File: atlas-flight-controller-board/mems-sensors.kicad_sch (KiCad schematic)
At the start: 11 parts, among them IC1 LSM6DSV80XTR, IC2 LPS22HHTR, U1 LIS2MDL

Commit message: Bare Schematic (No LEDS, etc added) finished. Begin PCB Layout.
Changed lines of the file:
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@@
+	)
+	(no_connect
+		(at 95.25 158.75)
+	)
+	(no_connect
+		(at 95.25 163.83)
+	)
+	(no_connect
+		(at 95.25 161.29)
 	)
 	(no_connect
 		(at 99.06 62.23)
 	)
-	(no_connect
-		(at 95.25 158.75)
-	)
-	(no_connect
-		(at 95.25 163.83)
-	)
-	(no_connect
-		(at 95.25 161.29)
-	)
 	(wire
 		(pts
@@
 	(wire
 		(pts
+			(xy 72.39 90.17) (xy 72.39 91.44)
+		)
+		(stroke
+			(width 0)
+			(type default)
+		)
+	)
+	(wire
+		(pts
 			(xy 83.82 87.63) (xy 83.82 91.44)
 		)
@@
 	(wire
 		(pts
-			(xy 73.66 90.17) (xy 73.66 91.44)
-		)
-		(stroke
-			(width 0)
-			(type default)
-		)
-	)
-	(wire
-		(pts
 			(xy 53.34 158.75) (xy 54.61 158.75)
 		)
@@
 	(wire
 		(pts
-			(xy 73.66 91.44) (xy 78.74 91.44)
+			(xy 72.39 91.44) (xy 78.74 91.44)
 		)
 		(stroke
@@
 	(wire
 		(pts
-			(xy 99.06 119.38) (xy 99.06 133.35)
+			(xy 99.06 127) (xy 99.06 133.35)
 		)
 		(stroke
@@
 	(symbol
 		(lib_id "power:+3V3")
-		(at 99.06 119.38 0)
-		(unit 1)
-		(exclude_from_sim no)
-		(in_bom yes)
-		(on_board yes)
-		(dnp no)
-		(fields_autoplaced yes)
-		(property "Reference" "#PWR0108"
-			(at 99.06 123.19 0)
-			(effects
-				(font
-					(size 1.27 1.27)
-				)
-				(hide yes)
-			)
-		)
-		(property "Value" "+3V3"
-			(at 99.06 114.3 0)
-			(effects
-				(font
-					(size 1.27 1.27)
-				)
-			)
-		)
-		(property "Footprint" ""
-			(at 99.06 119.38 0)
-			(effects
-				(font
-					(size 1.27 1.27)
-				)
-				(hide yes)
-			)
-		)
-		(property "Datasheet" ""
-			(at 99.06 119.38 0)
-			(effects
-				(font
-					(size 1.27 1.27)
-				)
-				(hide yes)
-			)
-		)
-		(property "Description" "Power symbol creates a global label with name \"+3V3\""
-			(at 99.06 119.38 0)
-			(effects
-				(font
-					(size 1.27 1.27)
-				)
-				(hide yes)
-			)
-		)
-		(pin "1"
-		)
-		(instances
-			(project "atlas-flight-controller-board"
-				(path "/99efb2d6-b5f7-438c-9ed2-f359400f01a1/5584e1ef-6e93-420a-9bdf-15a5926ce2b3"
-					(reference "#PWR0108")
-					(unit 1)
-				)
-			)
-		)
-	)
-	(symbol
-		(lib_id "power:+3V3")
 		(at 113.03 66.04 0)
 		(unit 1)
@@
 		(dnp no)
 		(fields_autoplaced yes)
-		(property "Reference" "#PWR0113"
+		(property "Reference" "#PWR010"
 			(at 113.03 69.85 0)
 			(effects
@@
 		)
 		(instances
-			(project "atlas-flight-controller-board"
+			(project ""
 				(path "/99efb2d6-b5f7-438c-9ed2-f359400f01a1/5584e1ef-6e93-420a-9bdf-15a5926ce2b3"
-					(reference "#PWR0113")
+					(reference "#PWR010")
 					(unit 1)
 				)
@@
 	(symbol
 		(lib_id "power:+3V3")
-		(at 182.88 38.1 0)
+		(at 99.06 127 0)
 		(unit 1)
 		(exclude_from_sim no)
@@
 		(dnp no)
 		(fields_autoplaced yes)
-		(property "Reference" "#PWR0105"
-			(at 182.88 41.91 0)
+		(property "Reference" "#PWR06"
+			(at 99.06 130.81 0)
 			(effects
 				(font
@@
 		)
 		(property "Value" "+3V3"
-			(at 182.88 33.02 0)
+			(at 99.06 121.92 0)
 			(effects
 				(font
@@
 		)
 		(property "Footprint" ""
-			(at 182.88 38.1 0)
+			(at 99.06 127 0)
 			(effects
 				(font
@@
 		)
 		(property "Datasheet" ""
-			(at 182.88 38.1 0)
+			(at 99.06 127 0)
 			(effects
 				(font
@@
 		)
 		(property "Description" "Power symbol creates a global label with name \"+3V3\""
-			(at 182.88 38.1 0)
+			(at 99.06 127 0)
 			(effects
 				(font
@@
 			(project "atlas-flight-controller-board"
 				(path "/99efb2d6-b5f7-438c-9ed2-f359400f01a1/5584e1ef-6e93-420a-9bdf-15a5926ce2b3"
-					(reference "#PWR0105")
+					(reference "#PWR06")
 					(unit 1)
 				)
@@
 	)
 	(symbol
-		(lib_id "power:+3V3")
-		(at 73.66 90.17 0)
-		(unit 1)
-		(exclude_from_sim no)
-		(in_bom yes)
-		(on_board yes)
-		(dnp no)
-		(fields_autoplaced yes)
-		(property "Reference" "#PWR0110"
-			(at 73.66 93.98 0)
-			(effects
-				(font
-					(size 1.27 1.27)
-				)
-				(hide yes)
-			)
-		)
-		(property "Value" "+3V3"
-			(at 73.66 85.09 0)
-			(effects
-				(font
-					(size 1.27 1.27)
-				)
-			)
-		)
-		(property "Footprint" ""
-			(at 73.66 90.17 0)
-			(effects
-				(font
-					(size 1.27 1.27)
-				)
-				(hide yes)
-			)
-		)
-		(property "Datasheet" ""
-			(at 73.66 90.17 0)
-			(effects
-				(font
-					(size 1.27 1.27)
-				)
-				(hide yes)
-			)
-		)
-		(property "Description" "Power symbol creates a global label with name \"+3V3\""
-			(at 73.66 90.17 0)
-			(effects
-				(font
-					(size 1.27 1.27)
-				)
-				(hide yes)
-			)
-		)
-		(pin "1"
-		)
-		(instances
-			(project "atlas-flight-controller-board"
-				(path "/99efb2d6-b5f7-438c-9ed2-f359400f01a1/5584e1ef-6e93-420a-9bdf-15a5926ce2b3"
-					(reference "#PWR0110")
-					(unit 1)
-				)
-			)
-		)
-	)
-	(symbol
 		(lib_id "power:GND")
 		(at 167.64 62.23 0)
@@
 	)
 	(symbol
+		(lib_id "power:+3V3")
+		(at 72.39 90.17 0)
+		(unit 1)
+		(exclude_from_sim no)
+		(in_bom yes)
+		(on_board yes)
+		(dnp no)
+		(fields_autoplaced yes)
+		(property "Reference" "#PWR013"
+			(at 72.39 93.98 0)
+			(effects
+				(font
+					(size 1.27 1.27)
+				)
+				(hide yes)
+			)
+		)
+		(property "Value" "+3V3"
+			(at 72.39 85.09 0)
+			(effects
+				(font
+					(size 1.27 1.27)
+				)
+			)
+		)
+		(property "Footprint" ""
+			(at 72.39 90.17 0)
+			(effects
+				(font
+					(size 1.27 1.27)
+				)
+				(hide yes)
+			)
+		)
+		(property "Datasheet" ""
+			(at 72.39 90.17 0)
+			(effects
+				(font
+					(size 1.27 1.27)
+				)
+				(hide yes)
+			)
+		)
+		(property "Description" "Power symbol creates a global label with name \"+3V3\""
+			(at 72.39 90.17 0)
+			(effects
+				(font
+					(size 1.27 1.27)
+				)
+				(hide yes)
+			)
+		)
+		(pin "1"
+		)
+		(instances
+			(project ""
+				(path "/99efb2d6-b5f7-438c-9ed2-f359400f01a1/5584e1ef-6e93-420a-9bdf-15a5926ce2b3"
+					(reference "#PWR013")
+					(unit 1)
+				)
+			)
+		)
+	)
+	(symbol
 		(lib_id "Device:C_Small")
 		(at 102.87 153.67 270)
@@
 					(unit 1)
 				)
+			)
+		)
+	)
+	(symbol
+		(lib_id "power:+3V3")
+		(at 182.88 38.1 0)
+		(unit 1)
+		(exclude_from_sim no)
+		(in_bom yes)
+		(on_board yes)
+		(dnp no)
+		(fields_autoplaced yes)
+		(property "Reference" "#PWR011"
+			(at 182.88 41.91 0)
+			(effects
+				(font
+					(size 1.27 1.27)
+				)
+				(hide yes)
+			)
+		)
+		(property "Value" "+3V3"
+			(at 182.88 33.02 0)
+			(effects
+				(font
+					(size 1.27 1.27)
+				)
+			)
+		)
+		(property "Footprint" ""
+			(at 182.88 38.1 0)
+			(effects
+				(font
+					(size 1.27 1.27)
+				)
+				(hide yes)
+			)
+		)
+		(property "Datasheet" ""
+			(at 182.88 38.1 0)
+			(effects
+				(font
+					(size 1.27 1.27)
+				)
+				(hide yes)
+			)
+		)
+		(property "Description" "Power symbol creates a global label with name \"+3V3\""
+			(at 182.88 38.1 0)
+			(effects
+				(font
+					(size 1.27 1.27)
+				)
+				(hide yes)
+			)
+		)
+		(pin "1"
+		)
+		(instances
+			(project "atlas-flight-controller-board"
+				(path "/99efb2d6-b5f7-438c-9ed2-f359400f01a1/5584e1ef-6e93-420a-9bdf-15a5926ce2b3"
+					(reference "#PWR011")
+					(unit 1)
+				)

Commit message: Re-arranging components, trying out different SPI routings
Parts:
- C3: footprint APA0606100M050R:CAP_APA_0606_AVX -> CAP_APA_0606_AVX; symbol APA0606100M050R:APA0606100M050R -> APA0606100M050R:_1
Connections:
- net +3V3: now also C3.1; no longer C3.+
- net GND: now also C3.2; no longer C3.-
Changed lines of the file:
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@@
+	)
+	(junction
+		(at 200.66 40.64)
+		(diameter 0)
+		(color 0 0 0 0)
+	)
+	(junction
+		(at 182.88 40.64)
+		(diameter 0)
+		(color 0 0 0 0)
+	)
+	(junction
+		(at 182.88 60.96)
+		(diameter 0)
+		(color 0 0 0 0)
 	)
 	(junction
@@
 	)
 	(junction
-		(at 200.66 40.64)
-		(diameter 0)
-		(color 0 0 0 0)
-	)
-	(junction
-		(at 182.88 40.64)
-		(diameter 0)
-		(color 0 0 0 0)
-	)
-	(junction
-		(at 182.88 60.96)
-		(diameter 0)
-		(color 0 0 0 0)
-	)
-	(junction
 		(at 107.95 153.67)
 		(diameter 0)
@@
 	(wire
 		(pts
-			(xy 106.68 133.35) (xy 107.95 133.35)
-		)
-		(stroke
-			(width 0)
-			(type default)
-		)
-	)
-	(wire
-		(pts
 			(xy 200.66 40.64) (xy 200.66 43.18)
 		)
@@
 	(wire
 		(pts
+			(xy 99.06 133.35) (xy 100.33 133.35)
+		)
+		(stroke
+			(width 0)
+			(type default)
+		)
+	)
+	(wire
+		(pts
 			(xy 81.28 87.63) (xy 83.82 87.63)
 		)
@@
 	(wire
 		(pts
+			(xy 99.06 127) (xy 99.06 133.35)
+		)
+		(stroke
+			(width 0)
+			(type default)
+		)
+	)
+	(wire
+		(pts
 			(xy 99.06 133.35) (xy 99.06 140.97)
 		)
@@
 	(wire
 		(pts
+			(xy 105.41 133.35) (xy 107.95 133.35)
+		)
+		(stroke
+			(width 0)
+			(type default)
+		)
+	)
+	(wire
+		(pts
 			(xy 107.95 148.59) (xy 107.95 153.67)
 		)
@@
 		(pts
 			(xy 113.03 69.85) (xy 113.03 71.12)
-		)
-		(stroke
-			(width 0)
-			(type default)
-		)
-	)
-	(wire
-		(pts
-			(xy 99.06 127) (xy 99.06 133.35)
 		)
 		(stroke
@@
 	)
 	(symbol
-		(lib_id "APA0606100M050R:APA0606100M050R")
-		(at 99.06 133.35 0)
+		(lib_id "APA0606100M050R:_1")
+		(at 102.87 130.81 0)
 		(unit 1)
 		(exclude_from_sim no)
@@
 		(dnp no)
 		(property "Reference" "C3"
-			(at 102.87 127 0)
+			(at 106.68 124.46 0)
 			(effects
 				(font
@@
 		)
 		(property "Value" "10 uF"
-			(at 102.87 130.556 0)
+			(at 102.87 130.81 0)
 			(effects
 				(font
@@
 			)
 		)
-		(property "Footprint" "APA0606100M050R:CAP_APA_0606_AVX"
-			(at 102.362 126.492 0)
-			(effects
-				(font
-					(size 1.27 1.27)
-					(italic yes)
+		(property "Footprint" "CAP_APA_0606_AVX"
+			(at 102.87 130.81 0)
+			(effects
+				(font
+					(size 1.27 1.27)
 				)
 				(hide yes)
@@
 		)
 		(property "Datasheet" "APA0606100M050R"
-			(at 102.616 128.27 0)
-			(effects
-				(font
-					(size 1.27 1.27)
-					(italic yes)
+			(at 102.87 130.81 0)
+			(effects
+				(font
+					(size 1.27 1.27)
 				)
 				(hide yes)
@@
 		)
 		(property "Description" ""
-			(at 99.06 133.35 0)
-			(effects
-				(font
-					(size 1.27 1.27)
-				)
-				(hide yes)
-			)
-		)
-		(pin "-"
-		)
-		(pin "+"
+			(at 102.87 130.81 0)
+			(effects
+				(font
+					(size 1.27 1.27)
+				)
+				(hide yes)
+			)
+		)
+		(pin "1"
+		)
+		(pin "2"
 		)
 		(instances

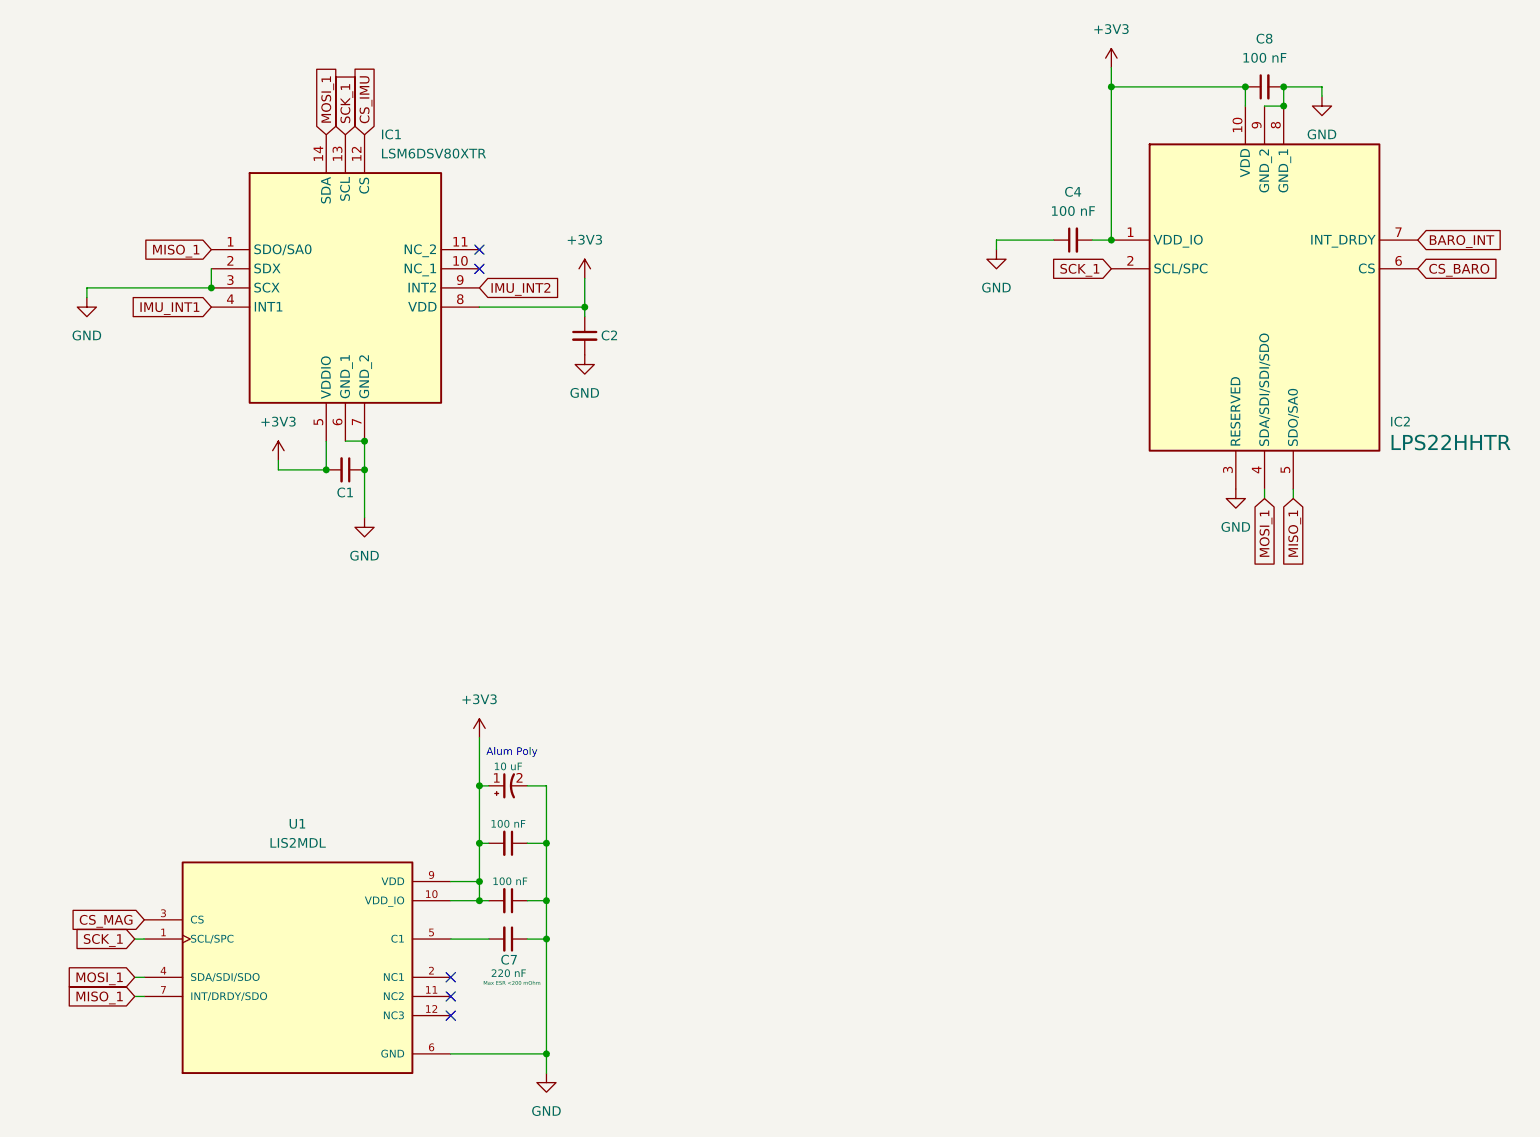
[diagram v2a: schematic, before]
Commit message: Sensor and Flash layout finished besides MISO, MOSI resistors (reduce ringing). Added plated M2 mounting holes.
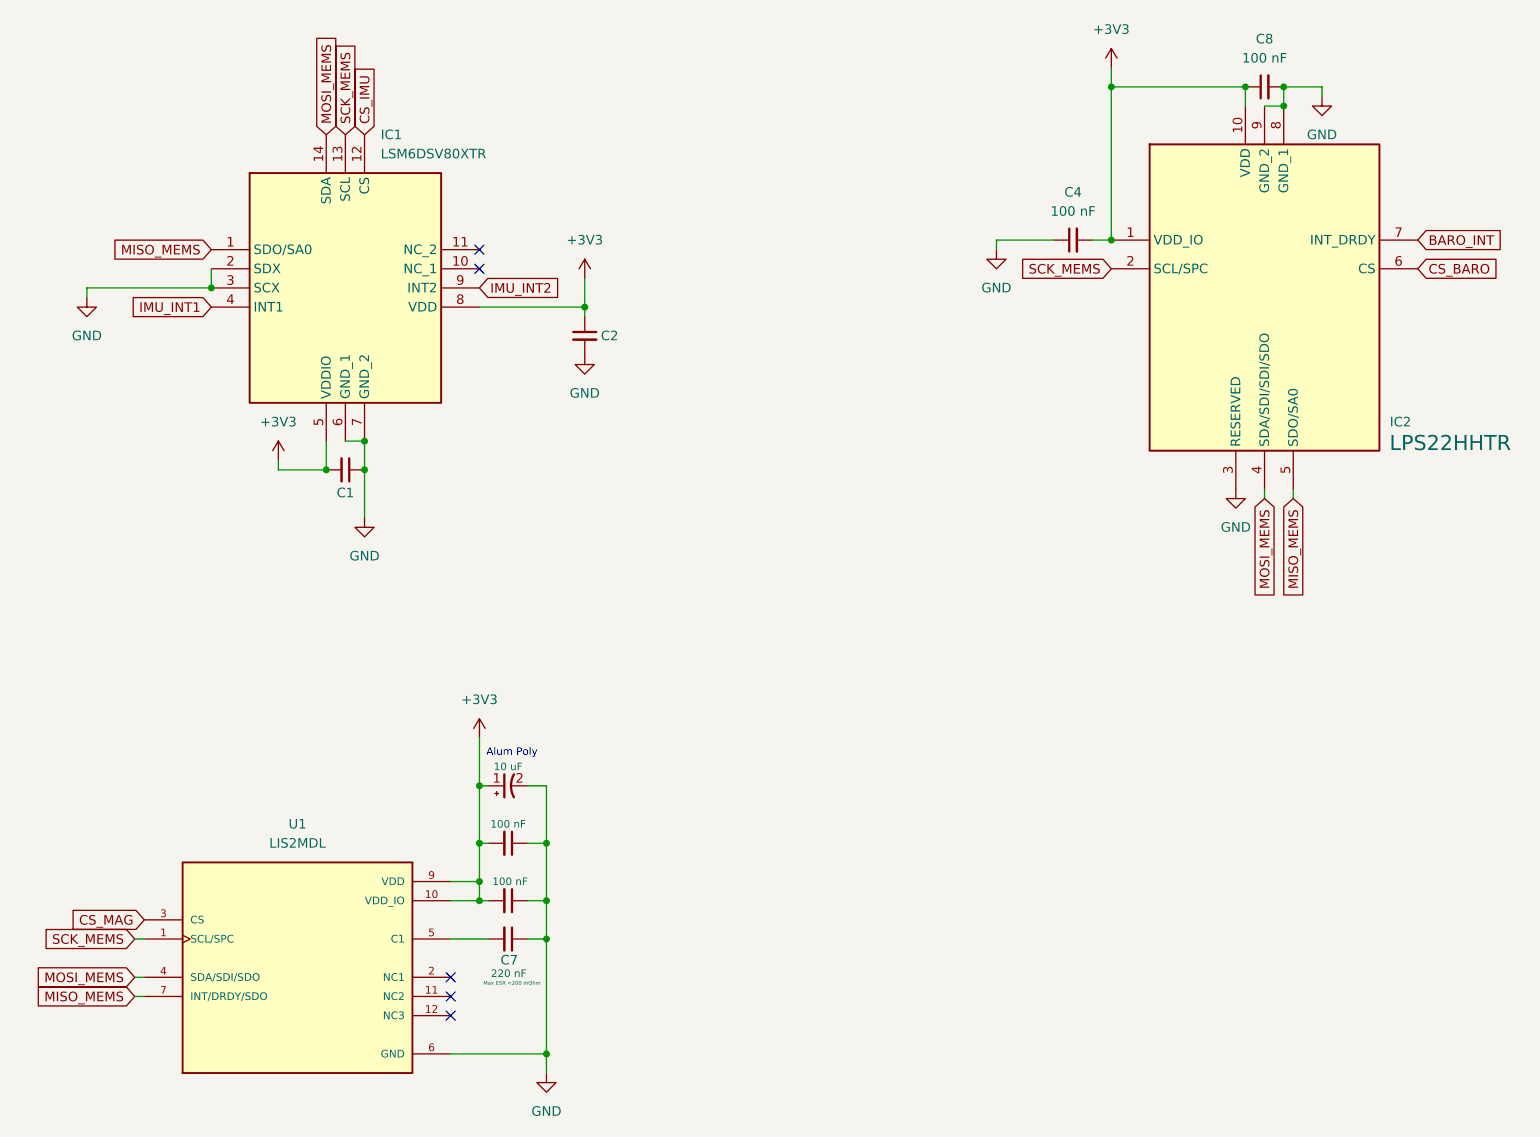
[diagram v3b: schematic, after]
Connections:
- net MISO_1 renamed MISO_MEMS
- net MOSI_1 renamed MOSI_MEMS
- net SCK_1 renamed SCK_MEMS
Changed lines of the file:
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@@
 		)
 	)
-	(global_label "SCK_1"
+	(global_label "SCK_MEMS"
 		(shape input)
 		(at 53.34 153.67 180)
@@
 		)
 		(property "Intersheetrefs" "${INTERSHEET_REFS}"
-			(at 44.4282 153.67 0)
-			(effects
-				(font
-					(size 1.27 1.27)
-				)
-				(justify right)
-				(hide yes)
-			)
-		)
-	)
-	(global_label "MISO_1"
+			(at 40.3764 153.67 0)
+			(effects
+				(font
+					(size 1.27 1.27)
+				)
+				(justify right)
+				(hide yes)
+			)
+		)
+	)
+	(global_label "MISO_MEMS"
 		(shape input)
 		(at 207.01 95.25 270)
@@
 		)
 		(property "Intersheetrefs" "${INTERSHEET_REFS}"
-			(at 207.01 105.0085 90)
-			(effects
-				(font
-					(size 1.27 1.27)
-				)
-				(justify right)
-				(hide yes)
-			)
-		)
-	)
-	(global_label "SCK_1"
+			(at 207.01 109.0603 90)
+			(effects
+				(font
+					(size 1.27 1.27)
+				)
+				(justify right)
+				(hide yes)
+			)
+		)
+	)
+	(global_label "SCK_MEMS"
 		(shape input)
 		(at 81.28 46.99 90)
@@
 		)
 		(property "Intersheetrefs" "${INTERSHEET_REFS}"
-			(at 81.28 38.0782 90)
+			(at 81.28 34.0264 90)
 			(effects
 				(font
@@
 		)
 	)
-	(global_label "MOSI_1"
+	(global_label "MOSI_MEMS"
 		(shape input)
 		(at 203.2 95.25 270)
@@
 		)
 		(property "Intersheetrefs" "${INTERSHEET_REFS}"
-			(at 203.2 105.0085 90)
-			(effects
-				(font
-					(size 1.27 1.27)
-				)
-				(justify right)
-				(hide yes)
-			)
-		)
-	)
-	(global_label "MISO_1"
+			(at 203.2 109.0603 90)
+			(effects
+				(font
+					(size 1.27 1.27)
+				)
+				(justify right)
+				(hide yes)
+			)
+		)
+	)
+	(global_label "MISO_MEMS"
 		(shape input)
 		(at 63.5 62.23 180)
@@
 		)
 		(property "Intersheetrefs" "${INTERSHEET_REFS}"
-			(at 53.7415 62.23 0)
-			(effects
-				(font
-					(size 1.27 1.27)
-				)
-				(justify right)
-				(hide yes)
-			)
-		)
-	)
-	(global_label "SCK_1"
+			(at 49.6897 62.23 0)
+			(effects
+				(font
+					(size 1.27 1.27)
+				)
+				(justify right)
+				(hide yes)
+			)
+		)
+	)
+	(global_label "SCK_MEMS"
 		(shape input)
 		(at 182.88 64.77 180)
@@
 		)
 		(property "Intersheetrefs" "${INTERSHEET_REFS}"
-			(at 173.9682 64.77 0)
+			(at 169.9164 64.77 0)
 			(effects
 				(font
@@
 		)
 	)
-	(global_label "MOSI_1"
+	(global_label "MOSI_MEMS"
 		(shape input)
 		(at 78.74 46.99 90)
@@
 		)
 		(property "Intersheetrefs" "${INTERSHEET_REFS}"
-			(at 78.74 37.2315 90)
-			(effects
-				(font
-					(size 1.27 1.27)
-				)
-				(justify left)
-				(hide yes)
-			)
-		)
-	)
-	(global_label "MISO_1"
+			(at 78.74 33.1797 90)
+			(effects
+				(font
+					(size 1.27 1.27)
+				)
+				(justify left)
+				(hide yes)
+			)
+		)
+	)
+	(global_label "MISO_MEMS"
 		(shape input)
 		(at 53.34 161.29 180)
@@
 		)
 		(property "Intersheetrefs" "${INTERSHEET_REFS}"
-			(at 43.5815 161.29 0)
+			(at 39.5297 161.29 0)
 			(effects
 				(font
@@
 		)
 	)
-	(global_label "MOSI_1"
+	(global_label "MOSI_MEMS"
 		(shape input)
 		(at 53.34 158.75 180)
@@
 		)
 		(property "Intersheetrefs" "${INTERSHEET_REFS}"
-			(at 43.5815 158.75 0)
-			(effects
-				(font
+			(at 39.5297 158.75 0)
+			(effects
+				(font

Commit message: Done.
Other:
- note added: "ALIGN IMU AND MAG IN SOFTWARE"
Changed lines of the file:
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@@
 	(generator_version "9.0")
 	(paper "A4")
+	(rectangle
+		(start 148.59 129.54)
+		(end 231.14 138.43)
+		(stroke
+			(width 0)
+			(type solid)
+		)
+		(fill
+			(type color)
+			(color 192 192 192 1)
+		)
+	)
+	(text "ALIGN IMU AND MAG IN SOFTWARE"
+		(exclude_from_sim no)
+		(at 189.738 133.858 0)
+		(effects
+			(font
+				(size 3 3)
+				(thickness 0.254)
+				(bold yes)
+			)
+		)
+	)
 	(text "Alum Poly\n"
 		(exclude_from_sim no)
